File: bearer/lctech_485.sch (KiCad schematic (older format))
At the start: 2 parts, among them P5 CONN_01X04, P6 CONN_01X04

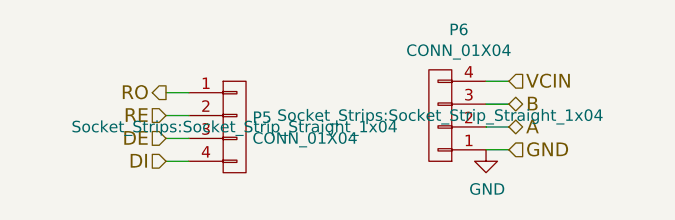
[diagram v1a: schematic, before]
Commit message: Low-side NPN switching. We'll see if things 'floating' causes issues... if so, I'll have to order a few PNP's to use for high-side switching.
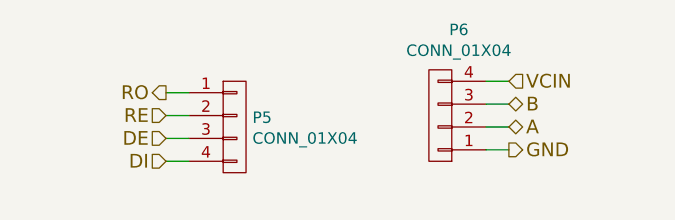
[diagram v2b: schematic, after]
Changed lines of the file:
@@
 Text HLabel 1200 1450 0    60   Input ~ 0
 DI
-Text HLabel 2700 1400 2    60   Input ~ 0
+Text HLabel 2700 1400 2    60   Output ~ 0
 GND
 Text HLabel 2700 1300 2    60   BiDi ~ 0
@@
 Text HLabel 2700 1200 2    60   BiDi ~ 0
 B
-$Comp
-L GND #PWR09
-U 1 1 588218CD
-P 2600 1400
-F 0 "#PWR09" H 2600 1150 50  0001 C CNN
-F 1 "GND" H 2605 1227 50  0000 C CNN
-F 2 "" H 2600 1400 50  0000 C CNN
-F 3 "" H 2600 1400 50  0000 C CNN
-	1    2600 1400
-	1    0    0    -1
-$EndComp
 Wire Wire Line
 	2700 1300 2600 1300
@@
 F 0 "P5" H 1578 1341 50  0000 L CNN
 F 1 "CONN_01X04" H 1578 1250 50  0000 L CNN
-F 2 "Socket_Strips:Socket_Strip_Straight_1x04" H 1500 1300 50  0000 C CNN
+F 2 "Socket_Strips:Socket_Strip_Straight_1x04" H 1500 1300 50  0001 C CNN
 F 3 "" H 1500 1300 50  0000 C CNN
 	1    1500 1300
@@
 F 0 "P6" H 2319 875 50  0000 C CNN
 F 1 "CONN_01X04" H 2319 966 50  0000 C CNN
-F 2 "Socket_Strips:Socket_Strip_Straight_1x04" H 2400 1250 50  0000 C CNN
+F 2 "Socket_Strips:Socket_Strip_Straight_1x04" H 2400 1250 50  0001 C CNN
 F 3 "" H 2400 1250 50  0000 C CNN
 	1    2400 1250
